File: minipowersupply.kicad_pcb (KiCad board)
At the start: 2 copper layers, 96.5 x 60.4 mm, 101 parts, among them J1 Conn_01x01_Female, J10 Conn_01x30_Male, J2 Conn_01x01_Female, J3 Conn_01x01_Female, J4 Conn_01x01_Female, J5 Conn_01x01_Female, J6 Conn_01x01_Female, J7 Conn_01x01_Female, J8 Conn_01x02_Female, J9 Conn_01x02_Female, Q1 BC817, SW1 RotaryEncoder_Switch, U1 ACS70331EOLCTR-2P5U3, U10 ACS70331EOLCTR-2P5U3, U11 74HC4051, U2 ACS70331EOLCTR-2P5U3, U3 ACS70331EOLCTR-2P5U3, U4 LM358, U5 74HC4051, U6 LM7805_TO220, U7 LM317L_TO92, U8 LM337L_TO92, U9 ACS70331EOLCTR-2P5U3

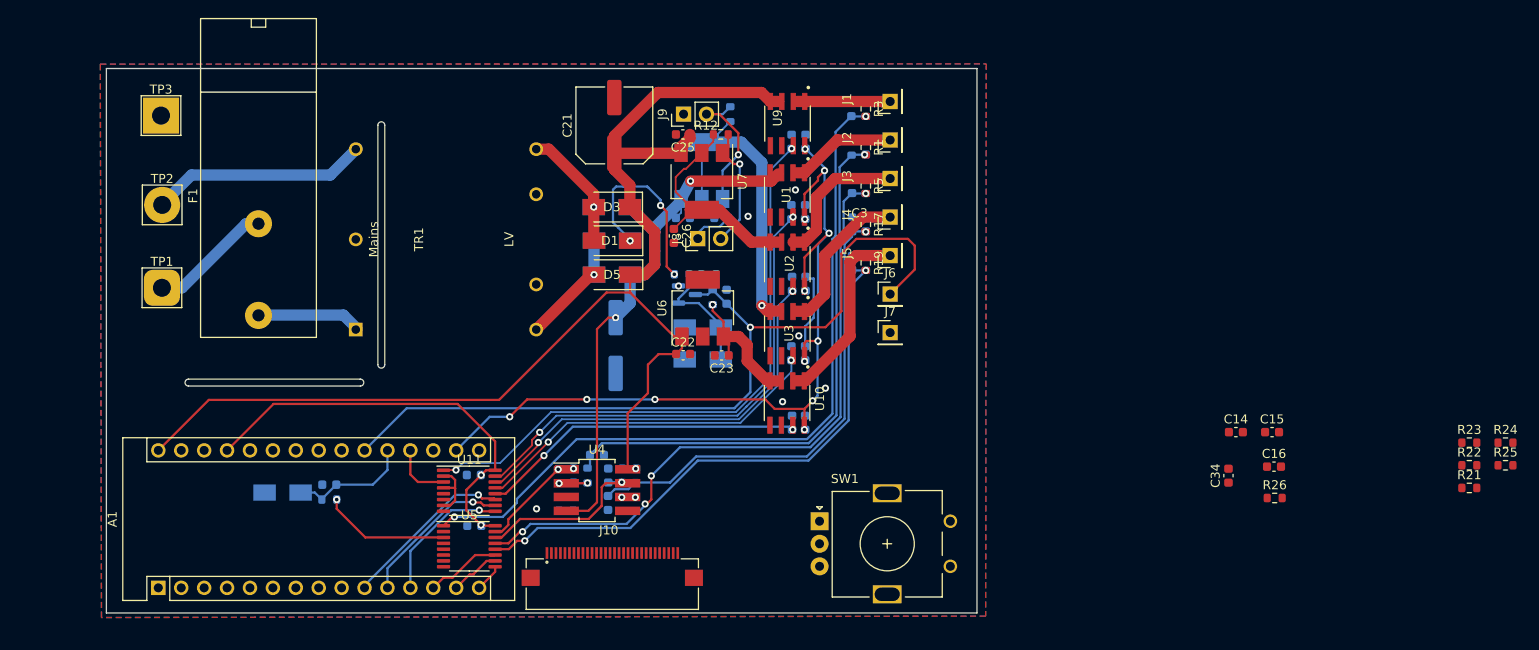
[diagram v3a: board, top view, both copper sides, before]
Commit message: adding diff and summing amps to scale amp inputs
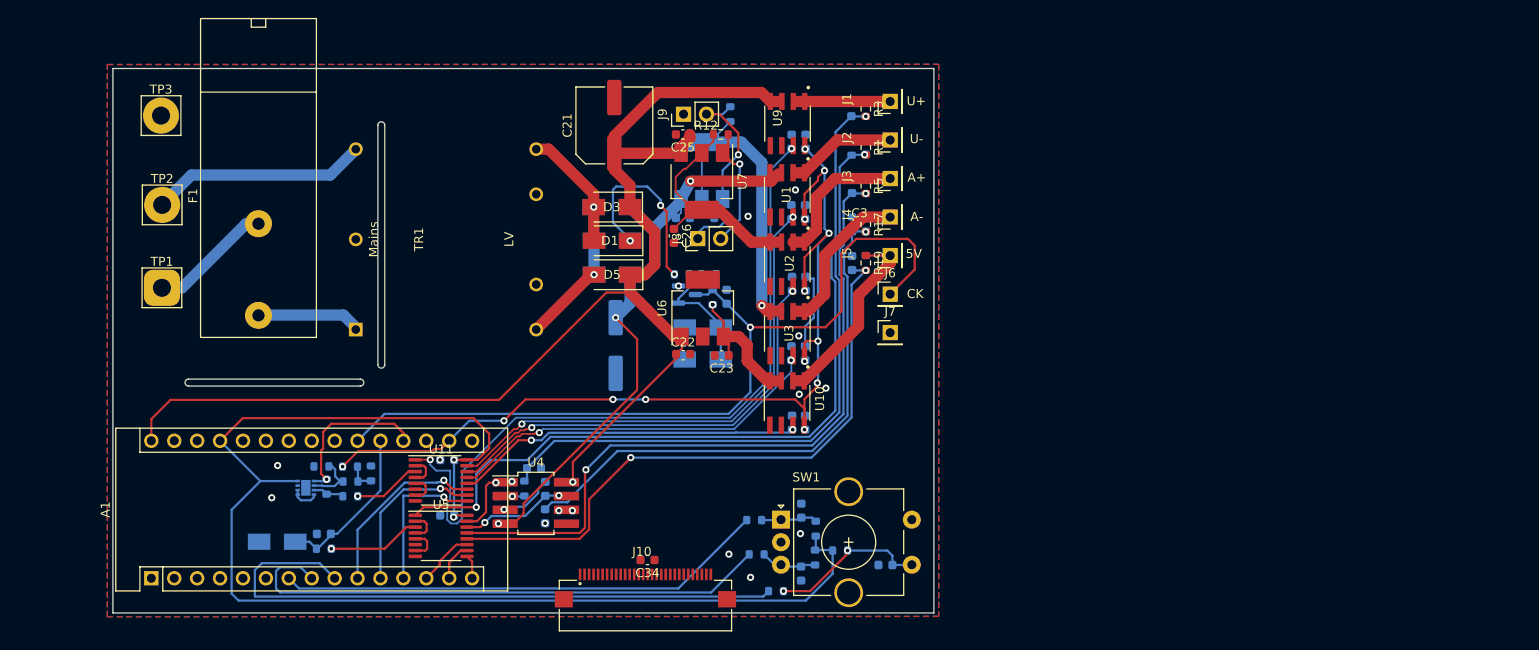
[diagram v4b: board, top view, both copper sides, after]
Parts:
- added R27: 100k, Resistor_SMD:R_0603_1608Metric, B.Cu at (111.0, 116.2)
- added R28: 10k, Resistor_SMD:R_0603_1608Metric, B.Cu at (113.7, 117.3)
- added R29: 10k, Resistor_SMD:R_0603_1608Metric, B.Cu at (113.7, 115.7)
- added R30: 10k, Resistor_SMD:R_0603_1608Metric, B.Cu at (113.7, 114.0)
- added R31: 10k, Resistor_SMD:R_0603_1608Metric, B.Cu at (116.0, 114.8)
- added R32: 100k, Resistor_SMD:R_0603_1608Metric, B.Cu at (110.5, 114.0)
- added U12: LM358_DFN, Package_DFN_QFN:DFN-8-1EP_2x2mm_P0.5mm_EP1.05x1.75mm, B.Cu at (108.8, 116.4)
- C14, C15, C16, R21, R22, R23, R24, R25, R26: moved to B.Cu
- SW1: footprint Rotary_Encoder:RotaryEncoder_Alps_EC11E_Vertical_H20mm -> Rotary_Encoder:RotaryEncoder_Alps_EC11E-Switch_Vertical_H20mm_CircularMountingHoles
- moved R22 79.6 mm to (158.7, 123.8), turned to 180 degrees
- moved R21 79.4 mm to (158.4, 120.0), turned to 180 degrees
- moved R23 78.6 mm to (160.9, 127.8)
- moved R24 77.1 mm to (165.3, 120.9), turned to 90 degrees
- moved R25 74.4 mm to (168.0, 123.3)
- moved C34 65.1 mm to (146.6, 124.4), turned to 180 degrees
- moved C15 52.9 mm to (163.7, 118.9), turned to 90 degrees
- moved R26 51.4 mm to (165.2, 124.1), turned to -90 degrees
- moved C14 50.7 mm to (163.7, 125.9), turned to 90 degrees
- moved C16 44.4 mm to (173.0, 124.9)
- moved C30 8.61 mm to (129.9, 116.5)
- moved R15 7.15 mm to (133.0, 116.5)
- moved R8 7.13 mm to (138.3, 118.1)
- moved C18 7.13 mm to (135.3, 119.5)
- moved R7 7.13 mm to (136.8, 118.1)
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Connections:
- net /I V Sensor and Mux/A0 renamed /I V Sensor, Mux and output/A0
- net /I V Sensor and Mux/A1 renamed /I V Sensor, Mux and output/A1
- net /I V Sensor and Mux/A2 renamed /I V Sensor, Mux and output/A2
- net /I V Sensor and Mux/A3 renamed /I V Sensor, Mux and output/A3
- net /I V Sensor and Mux/A4 renamed /I V Sensor, Mux and output/A4
- net /I V Sensor and Mux/A5 renamed /I V Sensor, Mux and output/A5
- net /I V Sensor and Mux/Curent and Volt4/Vout renamed /I V Sensor, Mux and output/Curent and Volt4/Vout
- net /I V Sensor and Mux/Curent and Volt5/Vout renamed /I V Sensor, Mux and output/Curent and Volt5/Vout
- net /I V Sensor and Mux/Curent and Volt6/Vout renamed /I V Sensor, Mux and output/Curent and Volt6/Vout
- net /I V Sensor and Mux/Curent and Volt7/Vout renamed /I V Sensor, Mux and output/Curent and Volt7/Vout
- net /I V Sensor and Mux/Curent and Volt8/Vout renamed /I V Sensor, Mux and output/Curent and Volt8/Vout
- net /I V Sensor and Mux/I5 renamed /I V Sensor, Mux and output/I5
- net /I V Sensor and Mux/IA+ renamed /I V Sensor, Mux and output/IA+
- net /I V Sensor and Mux/IA- renamed /I V Sensor, Mux and output/IA-
- net /I V Sensor and Mux/IU+ renamed /I V Sensor, Mux and output/IU+
- net /I V Sensor and Mux/IU- renamed /I V Sensor, Mux and output/IU-
- net /I V Sensor and Mux/Unity Inverter/Ain renamed /I V Sensor, Mux and output/Unity Inverter/Ain
- net /I V Sensor and Mux/Unity Inverter1/Ain renamed /I V Sensor, Mux and output/Unity Inverter1/Ain
- net /I V Sensor and Mux/V5+i renamed /I V Sensor, Mux and output/V5+i
- net /I V Sensor and Mux/VA+i renamed /I V Sensor, Mux and output/VA+i
- net /I V Sensor and Mux/VA-i renamed /I V Sensor, Mux and output/VA-i
- net /I V Sensor and Mux/VU+i renamed /I V Sensor, Mux and output/VU+i
- net /I V Sensor and Mux/VU-i renamed /I V Sensor, Mux and output/VU-i
- net /I V Sensor and Mux/Volt renamed /I V Sensor, Mux and output/Volt
- A1 pad 19: /I V Sensor and Mux/Amp -> Net-(A1-Pad19)
- U11 pad 3: /I V Sensor and Mux/Amp -> /I V Sensor, Mux and output/Amp
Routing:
- net V5: track 47.0 -> 144.0 mm
- net Net-(A1-Pad9): track 0.00 -> 70.0 mm
- net Net-(A1-Pad8): track 0.00 -> 61.0 mm
- net Net-(A1-Pad7): track 0.00 -> 54.4 mm
- net Net-(A1-Pad19): track 0.00 -> 17.6 mm, vias 0 -> 1
- net Net-(C16-Pad2): track 0.00 -> 17.6 mm, vias 0 -> 2
- net GNDREF: track 21.3 -> 37.7 mm, vias 7 -> 14
- net /I V Sensor, Mux and output/IU+: track 66.8 -> 82.4 mm
- net 3V3: track 90.9 -> 104.2 mm, vias 12 -> 13
- net /I V Sensor, Mux and output/VA-i: track 20.8 -> 12.5 mm, vias 1 -> 2
- net /I V Sensor, Mux and output/Unity Inverter1/Ain: track 52.4 -> 60.5 mm
- net /I V Sensor, Mux and output/Unity Inverter/Ain: track 62.0 -> 69.9 mm
- net /I V Sensor, Mux and output/Amp: track 0.00 -> 7.52 mm, vias 0 -> 1
- net /I V Sensor and Mux/Amp: track 6.69 -> 0.00 mm
- net Net-(C14-Pad2): track 0.00 -> 6.28 mm
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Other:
- board size 96.5 x 60.4 mm -> 91 x 60.4 mm
- board text added: "A+"
- board text added: "A-"
- board text added: "U+"
- board text added: "U-"
- board text removed: "VA+"
- board text removed: "VA-"
- board text removed: "VU+"
- board text removed: "VU-"

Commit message: added new op amps and used automated traces due to complexity
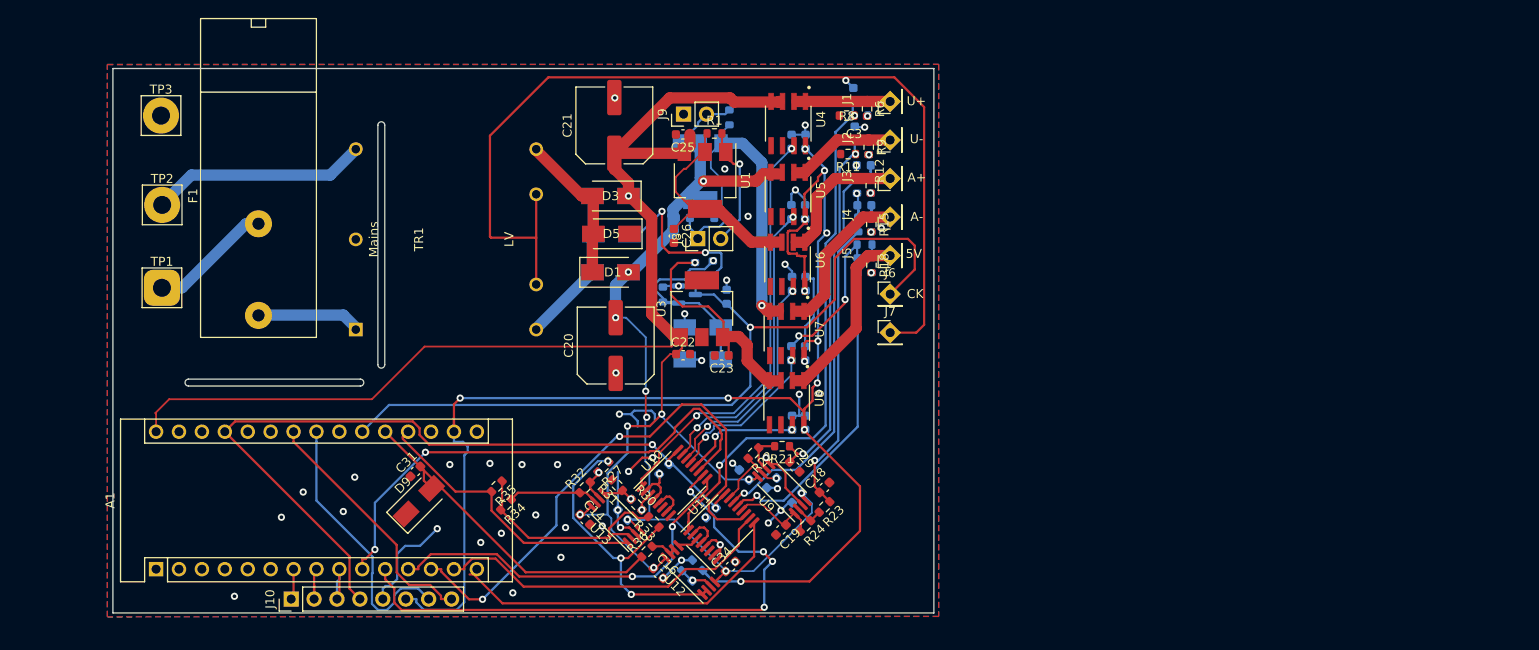
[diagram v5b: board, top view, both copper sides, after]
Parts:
- removed SW1: RotaryEncoder_Switch, Rotary_Encoder:RotaryEncoder_Alps_EC11E-Switch_Vertical_H20mm_CircularMountingHoles
- added R33: 10k 0.01%, Resistor_SMD:R_0603_1608Metric, F.Cu at (147.3, 120.1)
- added R34: 10k 0.01%, Resistor_SMD:R_0603_1608Metric, F.Cu at (130.9, 118.2)
- added R35: 10k 0.01%, Resistor_SMD:R_0603_1608Metric, F.Cu at (129.9, 116.2)
- added R36: 10k 0.01%, Resistor_SMD:R_0603_1608Metric, F.Cu at (146.6, 123.4)
- added U13: LM358, Package_SO:TSSOP-8_4.4x3mm_P0.65mm, F.Cu at (143.1, 119.8)
- C14, C16, C18, C19, C20, C29, C31, D9, R15, R18, R6, R8: moved to F.Cu
- J10: value Conn_01x30_Male -> Conn_01x08_Male; footprint WE SMD Side 30 Pin:687130149022 -> Connector_PinHeader_2.54mm:PinHeader_1x08_P2.54mm_Vertical
- R1: value 20k -> 240
- R10: value 4.420k -> 10k
- R11: value 698 -> 10k; moved to F.Cu
- R12, R13: value 240 -> 10k
- R17, R19: value 20k -> 10k; moved to B.Cu
- R2: value 10k -> 240
- R21, R22, R23, R24, R30: value 10k -> 10k 0.01%; moved to F.Cu
- R25, R26, R28, R29: value 10k -> 10k 0.01%
- R27: value 100k -> 10k 0.01%; moved to F.Cu
- R3: value 20k -> 4.420k; moved to B.Cu
- R31: value 10k -> 100k 0.01%; moved to F.Cu
- R32: value 100k -> 100k 0.01%; moved to F.Cu
- R4: value 10k -> 698
- R5: value 20k -> 410; moved to B.Cu
- R9: value 410 -> 10k; moved to F.Cu
- U1: value ACS70331EOLCTR-2P5U3 -> LM317_TO-220; footprint ACS70331EOLCTR-2P5U3:SOIC127P600X175-8N -> Package_TO_SOT_SMD:SOT-223-3_TabPin2
- U10: value ACS70331EOLCTR-2P5U3 -> 74HC4051; footprint ACS70331EOLCTR-2P5U3:SOIC127P600X175-8N -> Package_SO:TSSOP-16_4.4x5mm_P0.65mm
- U12: value LM358_DFN -> LM358; footprint Package_DFN_QFN:DFN-8-1EP_2x2mm_P0.5mm_EP1.05x1.75mm -> Package_SO:TSSOP-8_4.4x3mm_P0.65mm; moved to F.Cu
- U2: value ACS70331EOLCTR-2P5U3 -> LM337_TO220; footprint ACS70331EOLCTR-2P5U3:SOIC127P600X175-8N -> Package_TO_SOT_SMD:SOT-223-3_TabPin2; moved to B.Cu
- U3: value ACS70331EOLCTR-2P5U3 -> LM7805_TO220; footprint ACS70331EOLCTR-2P5U3:SOIC127P600X175-8N -> Package_TO_SOT_SMD:SOT-223-3_TabPin2
- U4: value LM358 -> ACS70331EOLCTR-2P5U3; footprint Package_TO_SOT_SMD:SOT-223-8 -> ACS70331EOLCTR-2P5U3:SOIC127P600X175-8N
- U5: value 74HC4051 -> ACS70331EOLCTR-2P5U3; footprint Package_SO:TSSOP-16_4.4x5mm_P0.65mm -> ACS70331EOLCTR-2P5U3:SOIC127P600X175-8N
- U6: value LM7805_TO220 -> ACS70331EOLCTR-2P5U3; footprint Package_TO_SOT_SMD:SOT-223-3_TabPin2 -> ACS70331EOLCTR-2P5U3:SOIC127P600X175-8N
- U7: value LM317L_TO92 -> ACS70331EOLCTR-2P5U3; footprint Package_TO_SOT_SMD:SOT-223-3_TabPin2 -> ACS70331EOLCTR-2P5U3:SOIC127P600X175-8N
- U8: value LM337L_TO92 -> ACS70331EOLCTR-2P5U3; footprint Package_TO_SOT_SMD:SOT-223-3_TabPin2 -> ACS70331EOLCTR-2P5U3:SOIC127P600X175-8N; moved to F.Cu
- U9: value ACS70331EOLCTR-2P5U3 -> LM358; footprint ACS70331EOLCTR-2P5U3:SOIC127P600X175-8N -> Package_SO:TSSOP-8_4.4x3mm_P0.65mm
- moved R16 70.5 mm to (171.4, 87.2), turned to 90 degrees
- moved R7 54.4 mm to (170.2, 75.1), turned to 180 degrees
- moved U5 54.0 mm to (162.2, 83.9), turned to -90 degrees
- moved R8 52.6 mm to (168.7, 75.1), turned to 180 degrees
- moved R14 50.9 mm to (169.8, 82.9), turned to -90 degrees
- moved U4 50.5 mm to (162.2, 76.0), turned to -90 degrees
- moved R15 48.3 mm to (171.4, 87.2)
- moved U12 43.6 mm to (151.4, 125.5), turned to 135 degrees
- moved U9 40.5 mm to (161.5, 116.5), turned to 135 degrees
- moved J10 39.4 mm to (107.1, 128.7), turned to 90 degrees
- moved C12 32.4 mm to (163.2, 117.5), turned to -135 degrees
- moved R30 32.0 mm to (145.4, 118.2), turned to -45 degrees
- moved R29 31.8 mm to (145.4, 118.2), turned to -45 degrees
- moved U11 31.5 mm to (154.8, 120.7), turned to 45 degrees
- moved C18 31.1 mm to (166.2, 116.3), turned to 45 degrees
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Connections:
- A1 pad 21: /Clock and TTL/CK_Out -> /Clock and TTL/Ck_Out
- A1 pad 23: /Measure and Display/SDA -> /Measure/SDA
- A1 pad 24: /Measure and Display/SCL -> /Measure/SCL
- A1 pad 30: /Clock and TTL/VUnreg+ -> VUnreg+
- C10 pad 1: /I V Sensor, Mux and output/Unity Inverter1/Ain -> /I V Sensor, Mux and output/A- Unity Inverter/Ain
- C11 pad 1: /Clock and TTL/VUnreg+ -> VUnreg+
- C12 pad 1: /DualAdj/VUnreg- -> VUnreg-
- C13 pad 1: /I V Sensor, Mux and output/V5+i -> /I V Sensor, Mux and output/V5+
- C14 pad 1: GNDREF -> VUnreg+
- C14 pad 2: Net-(C14-Pad2) -> GNDREF
- C15 pad 1: Net-(C15-Pad1) -> VUnreg-
- C16 pad 1: GNDREF -> VUnreg+
- C16 pad 2: Net-(C16-Pad2) -> GNDREF
- C18 pad 1: /I V Sensor, Mux and output/Unity Inverter1/Ain -> /I V Sensor, Mux and output/A- Unity Inverter/Ain
- C19 pad 1: /I V Sensor, Mux and output/VA-i -> /I V Sensor, Mux and output/VA-
- C20 pad 2: /DualAdj/VUnreg- -> VUnreg-
- C21 pad 1: /Clock and TTL/VUnreg+ -> VUnreg+
- C22 pad 1: /Clock and TTL/VUnreg+ -> VUnreg+
- C24 pad 1: /Clock and TTL/CK_Out -> /Clock and TTL/Ck_Out
- C25 pad 1: /Clock and TTL/VUnreg+ -> VUnreg+
- C27 pad 1: /DualAdj/VUnreg- -> VUnreg-
- C29 pad 1: /I V Sensor, Mux and output/Unity Inverter/Ain -> /I V Sensor, Mux and output/U- Unity Inverter/Ain
- C3 pad 1: /I V Sensor, Mux and output/Unity Inverter/Ain -> /I V Sensor, Mux and output/U- Unity Inverter/Ain
- C30 pad 1: /I V Sensor, Mux and output/VU-i -> /I V Sensor, Mux and output/VU-
- C34 pad 1: Net-(C34-Pad1) -> VUnreg-
- C6 pad 1: /I V Sensor, Mux and output/VU+i -> /I V Sensor, Mux and output/VU+
- C9 pad 1: /I V Sensor, Mux and output/VA+i -> /I V Sensor, Mux and output/VA+
- D1 pad 1: /Clock and TTL/HalfSineIn -> Net-(D1-Pad1)
- D1 pad 2: Net-(D1-Pad2) -> VUnreg-
- D2 pad 1: Net-(D1-Pad2) -> Net-(D2-Pad1)
- D2 pad 2: /DualAdj/VUnreg- -> VUnreg-
- D3 pad 1: /Clock and TTL/VUnreg+ -> VUnreg+
- D3 pad 2: Net-(D1-Pad2) -> Net-(D1-Pad1)
- D4 pad 1: Net-(D4-Pad1) -> VUnreg+
- D4 pad 2: /DualAdj/VUnreg- -> Net-(D2-Pad1)
- D5 pad 1: /Clock and TTL/VUnreg+ -> /Clock and TTL/HalfSineIn
- D5 pad 2: Net-(D4-Pad1) -> Net-(D1-Pad1)
- D6 pad 2: Net-(D4-Pad1) -> Net-(D2-Pad1)
- J1 pad 1: /I V Sensor, Mux and output/Curent and Volt4/Vout -> /I V Sensor, Mux and output/U+ Current/Vout
- J10 pad 1: GNDREF -> Net-(A1-Pad7)
- J10 pad 2: GNDREF -> Net-(A1-Pad8)
- J10 pad 3: unconnected-(J10-Pad3) -> Net-(A1-Pad9)
- J10 pad 4: unconnected-(J10-Pad4) -> V5
- J10 pad 5: Vdisp -> GNDREF
- J10 pad 6: unconnected-(J10-Pad6) -> 3V3
- J10 pad 7: unconnected-(J10-Pad7) -> /Measure/SDA
- J10 pad 8: unconnected-(J10-Pad8) -> /Measure/SCL
- J2 pad 1: /I V Sensor, Mux and output/Curent and Volt5/Vout -> /I V Sensor, Mux and output/U- Current/Vout
- J3 pad 1: /I V Sensor, Mux and output/Curent and Volt6/Vout -> /I V Sensor, Mux and output/A+ Current/Vout
- J4 pad 1: /I V Sensor, Mux and output/Curent and Volt7/Vout -> /I V Sensor, Mux and output/A- Current/Vout
- J5 pad 1: /I V Sensor, Mux and output/Curent and Volt8/Vout -> /I V Sensor, Mux and output/5 Current/Vout
- J6 pad 1: /Clock and TTL/CK_Out -> /Clock and TTL/Ck_Out
- Q1 pad 3: /Clock and TTL/CK_Out -> /Clock and TTL/Ck_Out
- R1 pad 1: /I V Sensor, Mux and output/Curent and Volt5/Vout -> /DualAdj/Vreg+
- R1 pad 2: /I V Sensor, Mux and output/Unity Inverter/Ain -> Net-(J8-Pad2)
- R10 pad 1: Net-(D7-Pad2) -> Net-(R10-Pad1)
- R10 pad 2: /Clock and TTL/HalfSineIn -> /I V Sensor, Mux and output/U- Unity Inverter/Ain
- R11 pad 1: Net-(D7-Pad2) -> /I V Sensor, Mux and output/U- Unity Inverter/Ain
- R12 pad 1: /DualAdj/Vreg+ -> /I V Sensor, Mux and output/A+ Current/Vout
- R12 pad 2: Net-(J8-Pad2) -> Net-(R12-Pad2)
- R13 pad 1: /DualAdj/Vreg- -> Net-(R12-Pad2)
- R13 pad 2: Net-(J9-Pad2) -> /I V Sensor, Mux and output/VA+
- R14 pad 1: Net-(R14-Pad1) -> /I V Sensor, Mux and output/VA+
- R14 pad 2: /I V Sensor, Mux and output/VU-i -> GNDREF
- R15 pad 1: /I V Sensor, Mux and output/Unity Inverter/Ain -> /I V Sensor, Mux and output/A- Current/Vout
- R15 pad 2: Net-(R14-Pad1) -> Net-(R15-Pad2)
- R16 pad 1: Net-(A1-Pad20) -> Net-(R15-Pad2)
- R16 pad 2: /I V Sensor, Mux and output/Volt -> /I V Sensor, Mux and output/A- Unity Inverter/Ain
- R17 pad 1: /I V Sensor, Mux and output/Curent and Volt7/Vout -> /I V Sensor, Mux and output/A- Unity Inverter/Ain
- R17 pad 2: /I V Sensor, Mux and output/Unity Inverter1/Ain -> GNDREF
- R18 pad 1: /I V Sensor, Mux and output/Unity Inverter1/Ain -> /I V Sensor, Mux and output/5 Current/Vout
- R18 pad 2: GNDREF -> Net-(R18-Pad2)
- R19 pad 1: /I V Sensor, Mux and output/Curent and Volt8/Vout -> Net-(R18-Pad2)
- R19 pad 2: /I V Sensor, Mux and output/V5+i -> /I V Sensor, Mux and output/V5+
- R2 pad 1: /I V Sensor, Mux and output/Unity Inverter/Ain -> /DualAdj/Vreg-
- R2 pad 2: GNDREF -> Net-(J9-Pad2)
- R20 pad 1: /I V Sensor, Mux and output/V5+i -> /I V Sensor, Mux and output/V5+
- R21 pad 1: Net-(C15-Pad1) -> /I V Sensor, Mux and output/U- Unity Inverter/Ain
- R21 pad 2: Net-(A1-Pad7) -> Net-(R21-Pad2)
- R22 pad 1: Net-(C14-Pad2) -> Net-(R21-Pad2)
- R22 pad 2: Net-(A1-Pad8) -> /I V Sensor, Mux and output/VU-
- R23 pad 1: Net-(A1-Pad9) -> /I V Sensor, Mux and output/A- Unity Inverter/Ain
- R23 pad 2: Net-(C16-Pad2) -> Net-(R23-Pad2)
- R24 pad 1: V5 -> Net-(R23-Pad2)
- R24 pad 2: Net-(C15-Pad1) -> /I V Sensor, Mux and output/VA-
- R25 pad 1: V5 -> 3V3
- R25 pad 2: Net-(C16-Pad2) -> Net-(R25-Pad2)
- R26 pad 1: V5 -> Net-(R25-Pad2)
- R26 pad 2: Net-(C14-Pad2) -> GNDREF
- R27 pad 1: Net-(A1-Pad19) -> Net-(R27-Pad1)
- R28 pad 1: Net-(R27-Pad2) -> Net-(R27-Pad1)
- R28 pad 2: /I V Sensor, Mux and output/Amp -> Net-(R27-Pad2)
- R29 pad 2: Net-(R29-Pad2) -> /I V Sensor, Mux and output/Amp
- R3 pad 1: /I V Sensor, Mux and output/Curent and Volt4/Vout -> Net-(D7-Pad2)
- R3 pad 2: /I V Sensor, Mux and output/VU+i -> /Clock and TTL/HalfSineIn
- R30 pad 1: 3V3 -> Net-(R29-Pad1)
- R30 pad 2: Net-(R29-Pad2) -> /I V Sensor, Mux and output/Amp
- R31 pad 1: Net-(R29-Pad2) -> Net-(R29-Pad1)
- R32 pad 1: Net-(R29-Pad1) -> Net-(R32-Pad1)
- R32 pad 2: GNDREF -> Net-(R27-Pad2)
- R4 pad 1: /I V Sensor, Mux and output/VU+i -> Net-(D7-Pad2)
- R5 pad 1: /I V Sensor, Mux and output/Curent and Volt6/Vout -> /Clock and TTL/V5Out
- R5 pad 2: /I V Sensor, Mux and output/VA+i -> /Clock and TTL/Ck_Out
- R6 pad 1: /I V Sensor, Mux and output/VA+i -> /I V Sensor, Mux and output/U+ Current/Vout
- R6 pad 2: GNDREF -> Net-(R6-Pad2)
- R7 pad 1: Net-(R7-Pad1) -> Net-(R6-Pad2)
- R7 pad 2: /I V Sensor, Mux and output/VA-i -> /I V Sensor, Mux and output/VU+
- R8 pad 1: /I V Sensor, Mux and output/Unity Inverter1/Ain -> /I V Sensor, Mux and output/VU+
- R8 pad 2: Net-(R7-Pad1) -> GNDREF
- R9 pad 1: /Clock and TTL/V5Out -> /I V Sensor, Mux and output/U- Current/Vout
- R9 pad 2: /Clock and TTL/CK_Out -> Net-(R10-Pad1)
- TR1 pad 3: Net-(D1-Pad2) -> Net-(D1-Pad1)
- TR1 pad 6: Net-(D4-Pad1) -> Net-(D2-Pad1)
- U1 pad 1: /I V Sensor, Mux and output/Curent and Volt5/Vout -> Net-(J8-Pad2)
- U1 pad 2: /I V Sensor, Mux and output/Curent and Volt5/Vout -> /DualAdj/Vreg+
- U1 pad 3: /DualAdj/VUnreg- -> VUnreg+
- U10 pad 1: /I V Sensor, Mux and output/Curent and Volt8/Vout -> /I V Sensor, Mux and output/IU+
- U10 pad 2: /I V Sensor, Mux and output/Curent and Volt8/Vout -> GNDREF
- U10 pad 3: /Clock and TTL/V5Out -> /I V Sensor, Mux and output/Amp
- U10 pad 4: /Clock and TTL/V5Out -> GNDREF
- U10 pad 7: /I V Sensor, Mux and output/I5 -> GNDREF
- U10 pad 8: 3V3 -> GNDREF
- U11 pad 1: /I V Sensor, Mux and output/IU+ -> /I V Sensor, Mux and output/VU+
- U11 pad 10: /I V Sensor, Mux and output/A1 -> /I V Sensor, Mux and output/A4
- U11 pad 11: /I V Sensor, Mux and output/A0 -> /I V Sensor, Mux and output/A3
- U11 pad 12: /I V Sensor, Mux and output/I5 -> /I V Sensor, Mux and output/VA-
- U11 pad 13: /I V Sensor, Mux and output/IA- -> /I V Sensor, Mux and output/V5+
- U11 pad 14: /I V Sensor, Mux and output/IA+ -> /I V Sensor, Mux and output/VA+
- U11 pad 15: /I V Sensor, Mux and output/IU- -> /I V Sensor, Mux and output/VU-
- U11 pad 3: /I V Sensor, Mux and output/Amp -> /I V Sensor, Mux and output/Volt
- U11 pad 9: /I V Sensor, Mux and output/A2 -> /I V Sensor, Mux and output/A5
- U12 pad 1: Net-(A1-Pad19) -> Net-(R27-Pad1)
- U12 pad 2: Net-(R29-Pad1) -> Net-(R27-Pad1)
- U12 pad 3: Net-(R27-Pad2) -> Net-(R25-Pad2)
- U12 pad 4: GNDREF -> VUnreg-
- U12 pad 5: GNDREF -> /I V Sensor, Mux and output/Volt
- U12 pad 6: GNDREF -> Net-(R36-Pad2)
- U12 pad 7: unconnected-(U12-Pad7) -> Net-(R36-Pad2)
- U12 pad 8: V5 -> VUnreg+
- U2 pad 1: /I V Sensor, Mux and output/Curent and Volt6/Vout -> Net-(J9-Pad2)
- U2 pad 2: /I V Sensor, Mux and output/Curent and Volt6/Vout -> VUnreg-
- U2 pad 3: /DualAdj/Vreg+ -> /DualAdj/Vreg-
- U3 pad 1: /I V Sensor, Mux and output/Curent and Volt7/Vout -> VUnreg+
- U3 pad 2: /I V Sensor, Mux and output/Curent and Volt7/Vout -> GNDREF
- U3 pad 3: /DualAdj/Vreg- -> /Clock and TTL/V5Out
- U4 pad 1: /I V Sensor, Mux and output/VU-i -> /I V Sensor, Mux and output/U+ Current/Vout
- U4 pad 2: Net-(R14-Pad1) -> /I V Sensor, Mux and output/U+ Current/Vout
- U4 pad 3: GNDREF -> VUnreg+
- U4 pad 4: /DualAdj/VUnreg- -> VUnreg+
- U4 pad 6: Net-(R7-Pad1) -> unconnected-(U4-Pad6)
- U4 pad 7: /I V Sensor, Mux and output/VA-i -> /I V Sensor, Mux and output/IU+
- U4 pad 8: /Clock and TTL/VUnreg+ -> 3V3
- U5 pad 1: /I V Sensor, Mux and output/VU+i -> /I V Sensor, Mux and output/U- Current/Vout
- U5 pad 2: GNDREF -> /I V Sensor, Mux and output/U- Current/Vout
- U5 pad 3: /I V Sensor, Mux and output/Volt -> VUnreg-
- U5 pad 4: GNDREF -> VUnreg-
- U5 pad 7: GNDREF -> /I V Sensor, Mux and output/IU-
- U5 pad 8: GNDREF -> 3V3
- U6 pad 1: /Clock and TTL/VUnreg+ -> /I V Sensor, Mux and output/A+ Current/Vout
- U6 pad 2: GNDREF -> /I V Sensor, Mux and output/A+ Current/Vout
- U6 pad 3: /Clock and TTL/V5Out -> /DualAdj/Vreg+
- U7 pad 1: Net-(J8-Pad2) -> /I V Sensor, Mux and output/A- Current/Vout
- U7 pad 2: /DualAdj/Vreg+ -> /I V Sensor, Mux and output/A- Current/Vout
- U7 pad 3: /Clock and TTL/VUnreg+ -> /DualAdj/Vreg-
- U8 pad 1: Net-(J9-Pad2) -> /I V Sensor, Mux and output/5 Current/Vout
- U8 pad 2: /DualAdj/Vreg- -> /I V Sensor, Mux and output/5 Current/Vout
- U8 pad 3: /DualAdj/VUnreg- -> /Clock and TTL/V5Out
- U9 pad 1: /I V Sensor, Mux and output/Curent and Volt4/Vout -> /I V Sensor, Mux and output/VA-
- U9 pad 2: /I V Sensor, Mux and output/Curent and Volt4/Vout -> Net-(R23-Pad2)
- U9 pad 3: /Clock and TTL/VUnreg+ -> GNDREF
- U9 pad 4: /Clock and TTL/VUnreg+ -> VUnreg-
- U9 pad 6: unconnected-(U9-Pad6) -> Net-(R21-Pad2)
- U9 pad 7: /I V Sensor, Mux and output/IU+ -> /I V Sensor, Mux and output/VU-
- U9 pad 8: 3V3 -> VUnreg+
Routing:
- net GNDREF: track 37.7 -> 230.3 mm, vias 14 -> 53
- net VUnreg+: track 0.00 -> 177.6 mm, vias 0 -> 6
- net /Clock and TTL/VUnreg+: track 142.2 -> 0.00 mm, vias 1 -> 0
- net VUnreg-: track 0.00 -> 95.7 mm, vias 0 -> 8
- net /Clock and TTL/CK_Out: track 93.8 -> 0.00 mm, vias 1 -> 0
- net /Clock and TTL/Ck_Out: track 0.00 -> 93.0 mm, vias 0 -> 1
- net /I V Sensor, Mux and output/VU+i: track 88.9 -> 0.00 mm, vias 2 -> 0
- net /I V Sensor, Mux and output/VA+i: track 77.9 -> 0.00 mm, vias 2 -> 0
- net /I V Sensor, Mux and output/Unity Inverter/Ain: track 69.9 -> 0.00 mm, vias 1 -> 0
- net /I V Sensor, Mux and output/V5+i: track 68.8 -> 0.00 mm, vias 2 -> 0
- net /DualAdj/VUnreg-: track 66.1 -> 0.00 mm, vias 3 -> 0
- net 3V3: track 104.2 -> 167.5 mm, vias 13 -> 12
- net Net-(A1-Pad9): track 70.0 -> 7.03 mm
- net /I V Sensor, Mux and output/VU+: track 0.00 -> 60.8 mm, vias 0 -> 2
- net /I V Sensor, Mux and output/Unity Inverter1/Ain: track 60.5 -> 0.00 mm, vias 1 -> 0
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
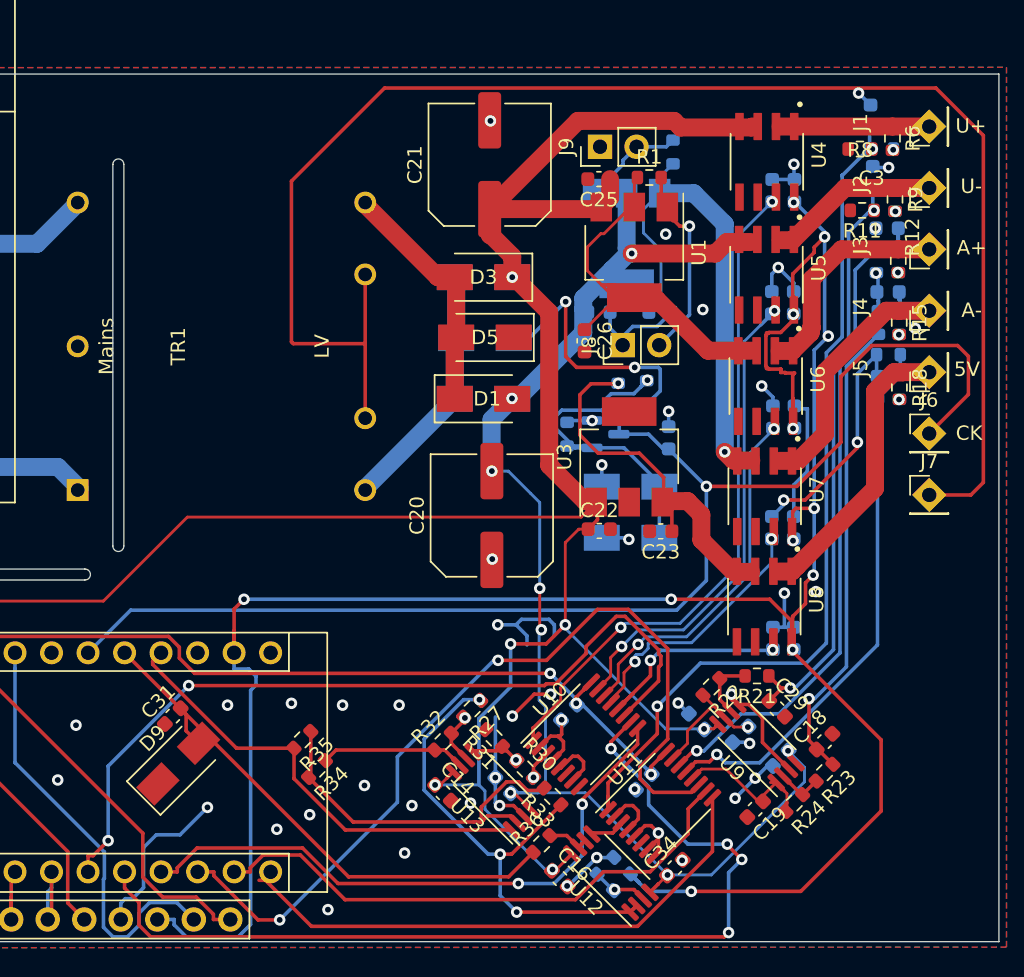
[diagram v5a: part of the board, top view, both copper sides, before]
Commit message: fixed last ground plane connection, added ground ring for power output ground
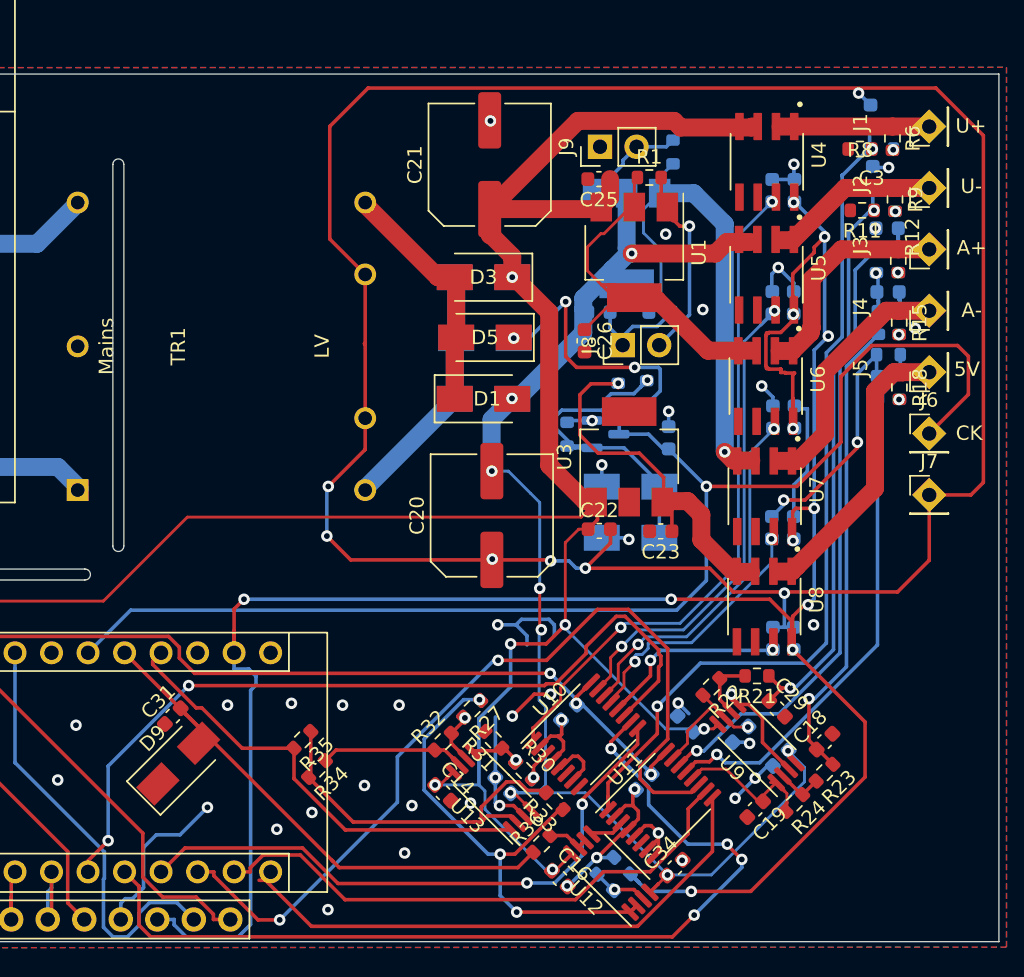
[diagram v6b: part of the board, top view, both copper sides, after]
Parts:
- R10, R11, R12, R13, R14, R15, R16, R17, R18, R19, R20, R6, R7, R8, R9: value 10k -> 10k 0.01%
- moved C11 0.80 mm to (156.6, 115.1)
- moved R33 0.36 mm to (147.5, 120.5)
- moved R31 0.14 mm to (143.2, 116.2)
- moved R29 0.13 mm to (145.3, 118.3)
- moved R30 0.13 mm to (145.3, 118.3)
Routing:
- net GNDREF: track 230.3 -> 287.0 mm, vias 53 -> 57
- net 3V3: track 167.5 -> 164.8 mm
- net /I V Sensor, Mux and output/A1: track 66.6 -> 64.5 mm
- net /Clock and TTL/HalfSineIn: vias 2 -> 3
